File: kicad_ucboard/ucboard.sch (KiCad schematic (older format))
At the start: 180 parts, among them IC1 FT232RL, P1 Powerpath In, P10 BATTERY 2, P11 Timer8, P12 Timer20, P13 USB_B, P14 CAR-ID, P15 JTAG, P16 DIO, P17 ADC, P18 MPU-9250_EXT, P19 SFR08_I2C, P2 PWM_SERVO, P20 I2C2, P21 I2C3, P22 Serial Port, P23 5V, P24 5V, P25 3.3V, P26 UART4, P27 SPI2, P28 SPI4, P29 5V_Servo, P3 PWM_DRIVE, P4 BATT2_IN, P5 ADC12, P6 BATT2_REG_OUT, P7 Timer1, P8 Timer3, P9 Hal5, Q1 IRLML9301, Q2 IRLML6344, Q3 IRLML6344, Q4 IRLML9301, Q5 IRLML9301, Q6 IRLML6344, SW1 RESET, SW2 Button1, SW3 Button2, SW4 Button3, U1 STM32F303VE, U2 TEN_30-1212, U3 MCP6054, U4 TSR_1-2450, U5 TSR_1-2450, U6 LD1117_S33TR, U7 MPU-9250, U8 MAX3232, U9 25LC160A-I/SN, Y1 8MHz

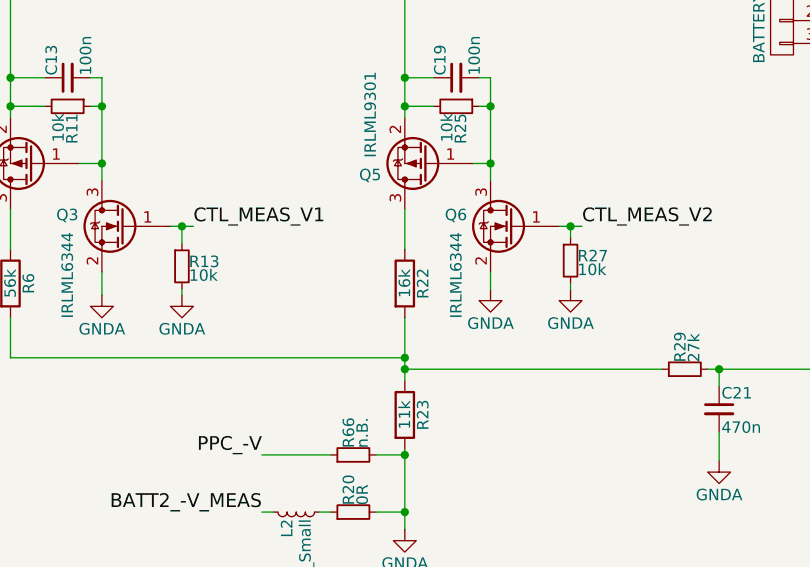
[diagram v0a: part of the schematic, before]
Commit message: - Bestellisten bis auf Spulen/Ferrite zur Entkopplung vervollständigt - Oberer Widerstand im Spannungsteiler an 7,2V von 16k auf 14k Reduziert (7,5V -> 3,3V)
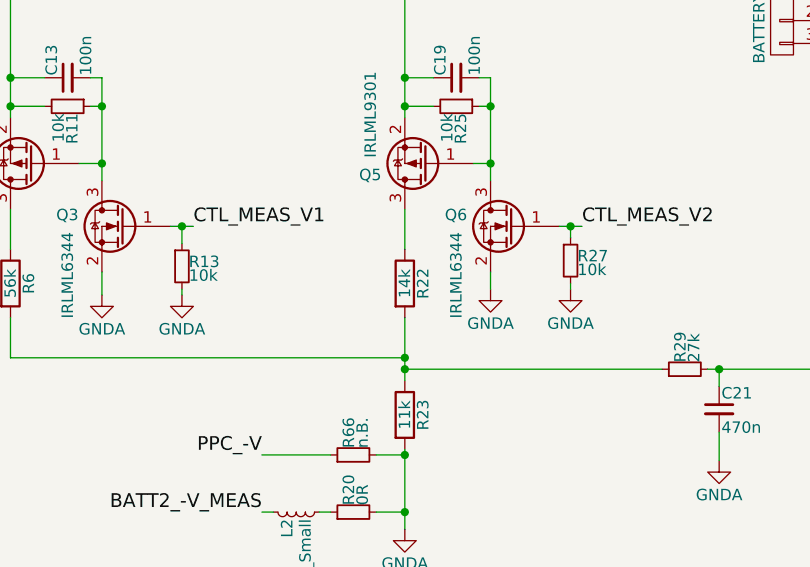
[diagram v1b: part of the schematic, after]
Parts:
- R22: value 16k -> 14k
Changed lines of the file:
@@
 EESchema Schematic File Version 2
-LIBS:ucboard-rescue
 LIBS:power
 LIBS:device
@@
 P 6675 4350
 F 0 "R22" V 6755 4350 50  0000 C CNN
-F 1 "16k" V 6675 4350 50  0000 C CNN
+F 1 "14k" V 6675 4350 50  0000 C CNN
 F 2 "Resistors_SMD:R_0603_HandSoldering" V 6605 4350 50  0001 C CNN
 F 3 "" H 6675 4350 50  0000 C CNN

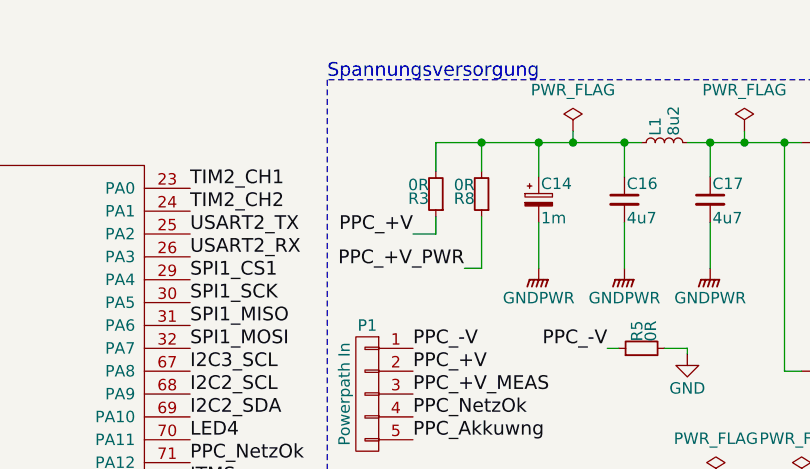
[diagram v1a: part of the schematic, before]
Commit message: - Wert von R3 von 0R auf n.B. geändert
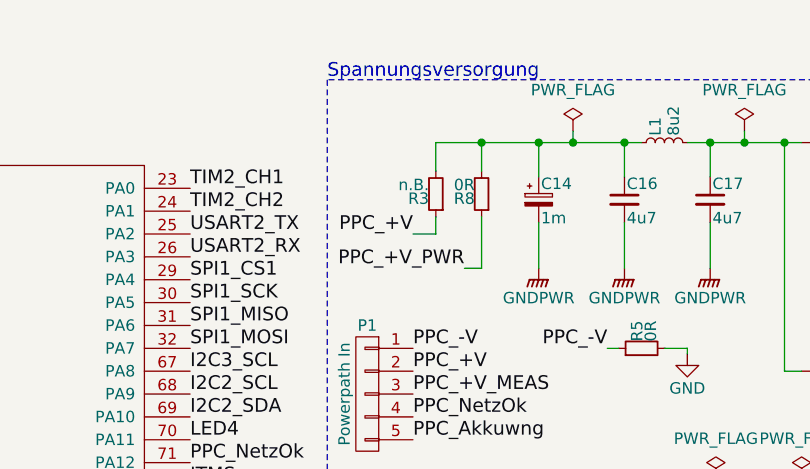
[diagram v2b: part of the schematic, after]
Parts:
- R3: value 0R -> n.B.
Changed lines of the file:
@@
 P 4825 1250
 F 0 "R3" H 4855 1270 50  0000 L CNN
-F 1 "0R" H 4855 1210 50  0000 L CNN
+F 1 "n.B." H 4855 1210 50  0000 L CNN
 F 2 "Resistors_SMD:R_0603_HandSoldering" H 4825 1250 50  0001 C CNN
 F 3 "" H 4825 1250 50  0000 C CNN

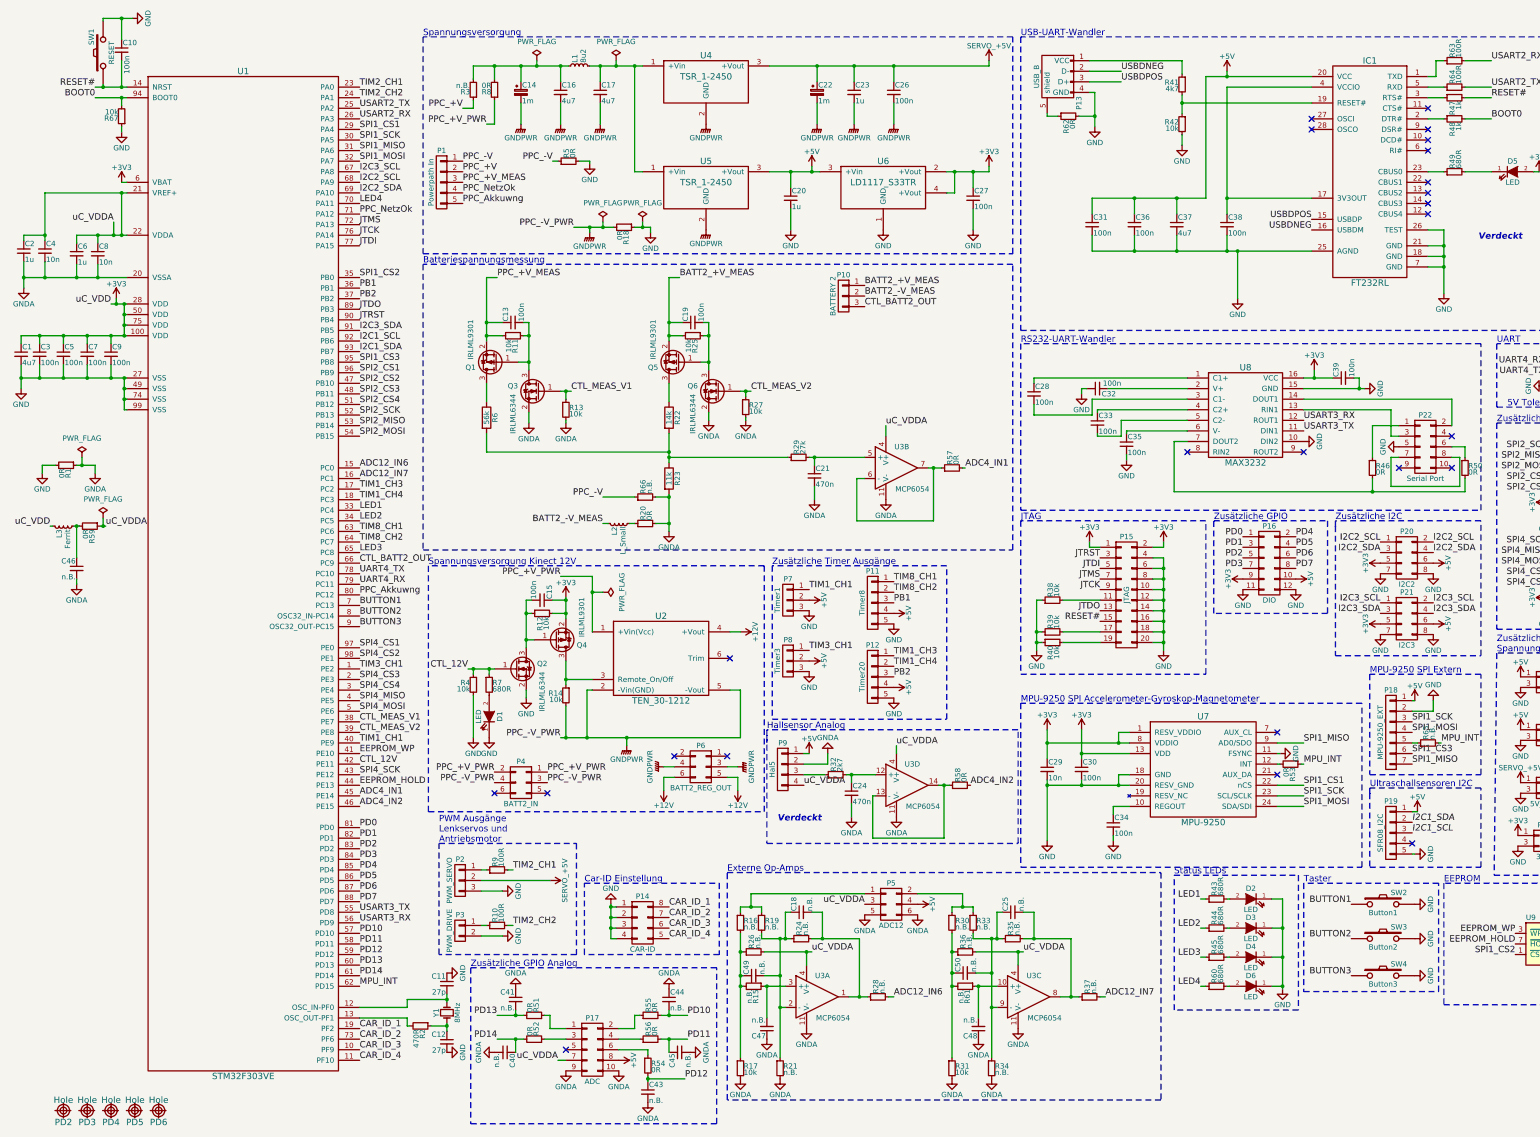
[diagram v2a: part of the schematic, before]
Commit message: Anpassen Schaltplan an aktuelle Bestückung: - R22: 56k anstelle 14k - C24: n.B. anstelle 470n - R68: 10k Pull-up für Hallsensor hinzugefügt
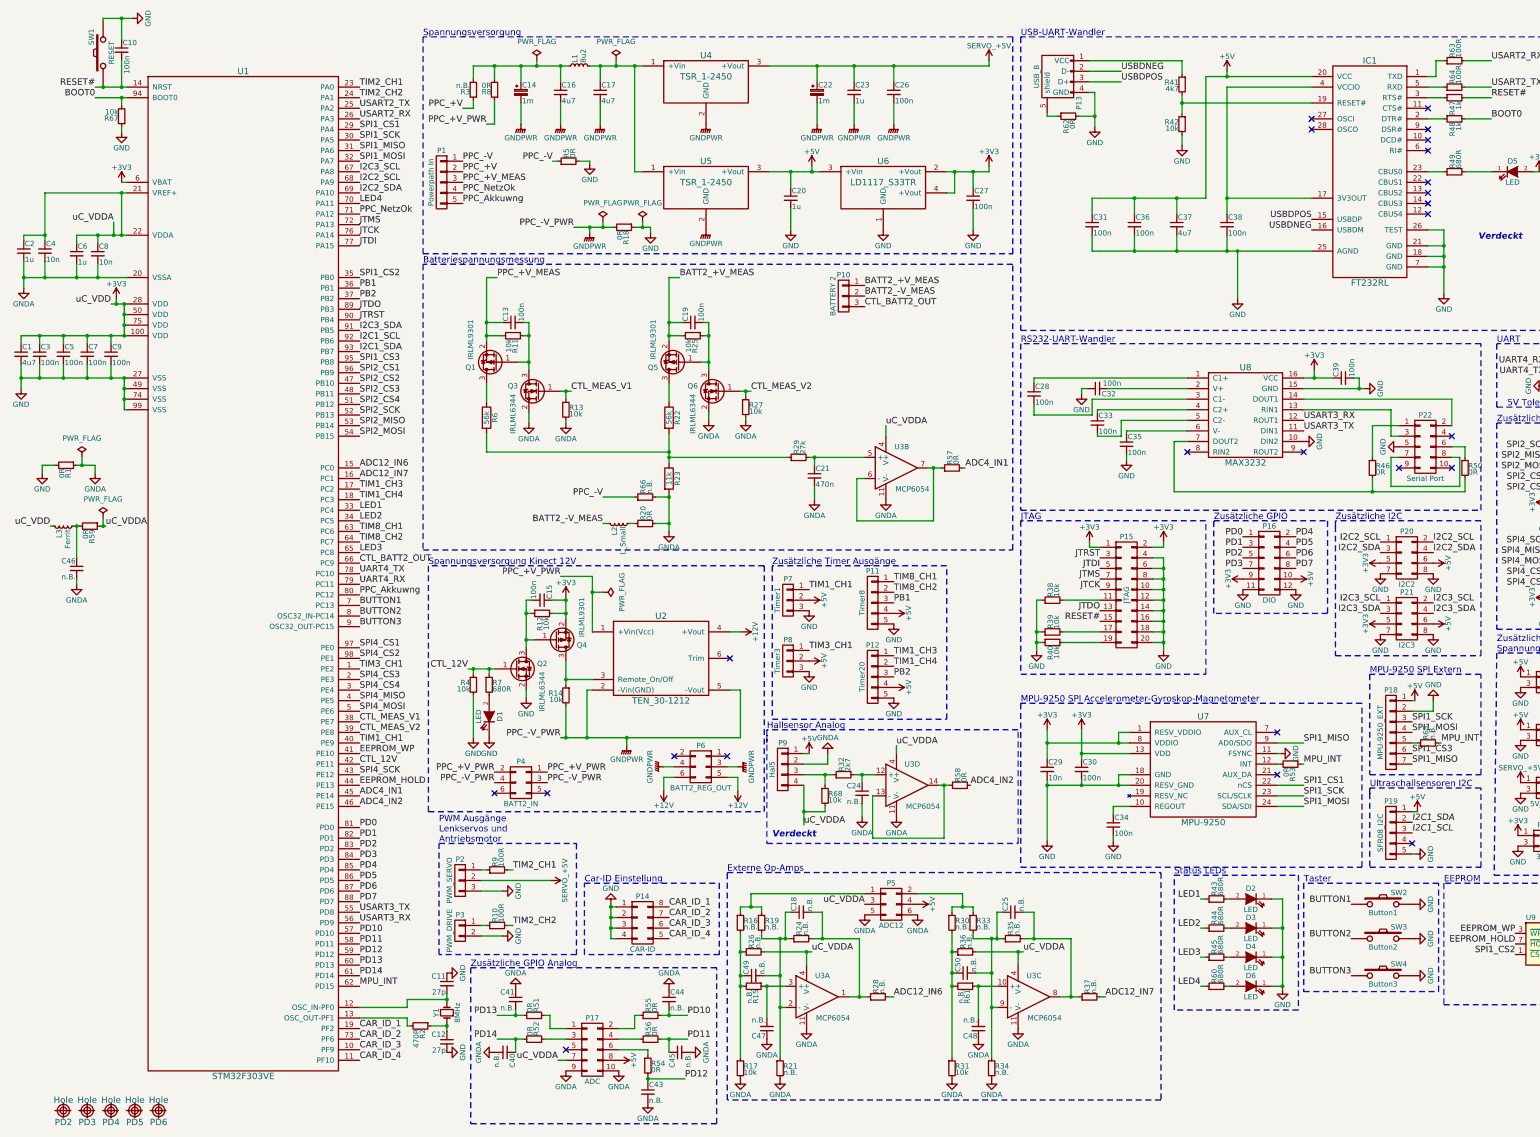
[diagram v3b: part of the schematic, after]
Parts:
- added R68: 10k, Resistors_SMD:R_0603_HandSoldering, symbol R_Small
- C24: value 470n -> n.B.
- R22: value 14k -> 56k; Supply (none) -> VEN:
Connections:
- net uC_VDDA: now also R68.2
- net at P9.3 (P3), R32.1: now also R68.1
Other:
- moved on the sheet: C24, R32

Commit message: In Kicad geänderte Bauteile "gerettet".
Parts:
- D1, D2, D3, D4, D5, D6: symbol LED -> LED-RESCUE-ucboard
- P13: symbol USB_B -> USB_B-RESCUE-ucboard
- U8: symbol MAX3232 -> MAX3232-RESCUE-ucboard

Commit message: Spezifikation D1-D6, L2+L3 nachgetragen
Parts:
- D1, D3: value LED -> 2mA, gn
- D2, D4, D5: value LED -> 2mA, re
- D6: value LED -> 2mA, or
- L2: value L_Small -> FB 600R; Supply (none) -> Farnell, 1635735
- L3: value Ferrit -> FB 600R; Supply (none) -> Farnell, 1635735
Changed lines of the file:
@@
 P 14650 2025
 F 0 "D5" H 14650 2125 50  0000 C CNN
-F 1 "LED" H 14650 1925 50  0000 C CNN
+F 1 "2mA, re" H 14650 1925 50  0000 C CNN
 F 2 "Custom:LED_0603_HandSoldering" H 14650 2025 50  0001 C CNN
 F 3 "" H 14650 2025 50  0000 C CNN
@@
 P 12175 9175
 F 0 "D3" H 12175 9275 50  0000 C CNN
-F 1 "LED" H 12175 9075 50  0000 C CNN
+F 1 "2mA, gn" H 12175 9075 50  0000 C CNN
 F 2 "Custom:LED_0603_HandSoldering" H 12175 9175 50  0001 C CNN
 F 3 "" H 12175 9175 50  0000 C CNN
@@
 P 12175 8900
 F 0 "D2" H 12175 9000 50  0000 C CNN
-F 1 "LED" H 12175 8800 50  0000 C CNN
+F 1 "2mA, re" H 12175 8800 50  0000 C CNN
 F 2 "Custom:LED_0603_HandSoldering" H 12175 8900 50  0001 C CNN
 F 3 "" H 12175 8900 50  0000 C CNN
@@
 P 12175 9450
 F 0 "D4" H 12175 9550 50  0000 C CNN
-F 1 "LED" H 12175 9350 50  0000 C CNN
+F 1 "2mA, re" H 12175 9350 50  0000 C CNN
 F 2 "Custom:LED_0603_HandSoldering" H 12175 9450 50  0001 C CNN
 F 3 "" H 12175 9450 50  0000 C CNN
@@
 P 4975 7175
 F 0 "D1" H 4975 7275 50  0000 C CNN
-F 1 "LED" H 4975 7075 50  0000 C CNN
+F 1 "2mA, gn" H 4975 7075 50  0000 C CNN
 F 2 "Custom:LED_0603_HandSoldering" H 4975 7175 50  0001 C CNN
 F 3 "" H 4975 7175 50  0000 C CNN
@@
 P 6200 5350
 F 0 "L2" H 6230 5390 50  0000 L CNN
-F 1 "L_Small" H 6230 5310 50  0000 L CNN
+F 1 "FB 600R" H 6230 5310 50  0000 L CNN
 F 2 "Resistors_SMD:R_0805_HandSoldering" H 6200 5350 50  0001 C CNN
 F 3 "" H 6200 5350 50  0000 C CNN
 F 4 "Spule oder Ferritperle" H 6200 5350 60  0001 C CNN "Spec"
+F 5 "Farnell, 1635735" H 6200 5350 60  0001 C CNN "Supply"
 	1    6200 5350
 	0    -1   1    0
@@
 P 950 5375
 F 0 "L3" H 980 5415 50  0000 L CNN
-F 1 "Ferrit" H 980 5335 50  0000 L CNN
+F 1 "FB 600R" H 980 5335 50  0000 L CNN
 F 2 "Resistors_SMD:R_0805_HandSoldering" H 950 5375 50  0001 C CNN
 F 3 "" H 950 5375 50  0000 C CNN
 F 4 "Spule oder Ferritperle" H 950 5375 60  0001 C CNN "Spec"
+F 5 "Farnell, 1635735" H 950 5375 60  0001 C CNN "Supply"
 	1    950  5375
 	0    -1   1    0
@@
 P 12175 9725
 F 0 "D6" H 12175 9825 50  0000 C CNN
-F 1 "LED" H 12175 9625 50  0000 C CNN
+F 1 "2mA, or" H 12175 9625 50  0000 C CNN
 F 2 "Custom:LED_0603_HandSoldering" H 12175 9725 50  0001 C CNN
 F 3 "" H 12175 9725 50  0000 C CNN

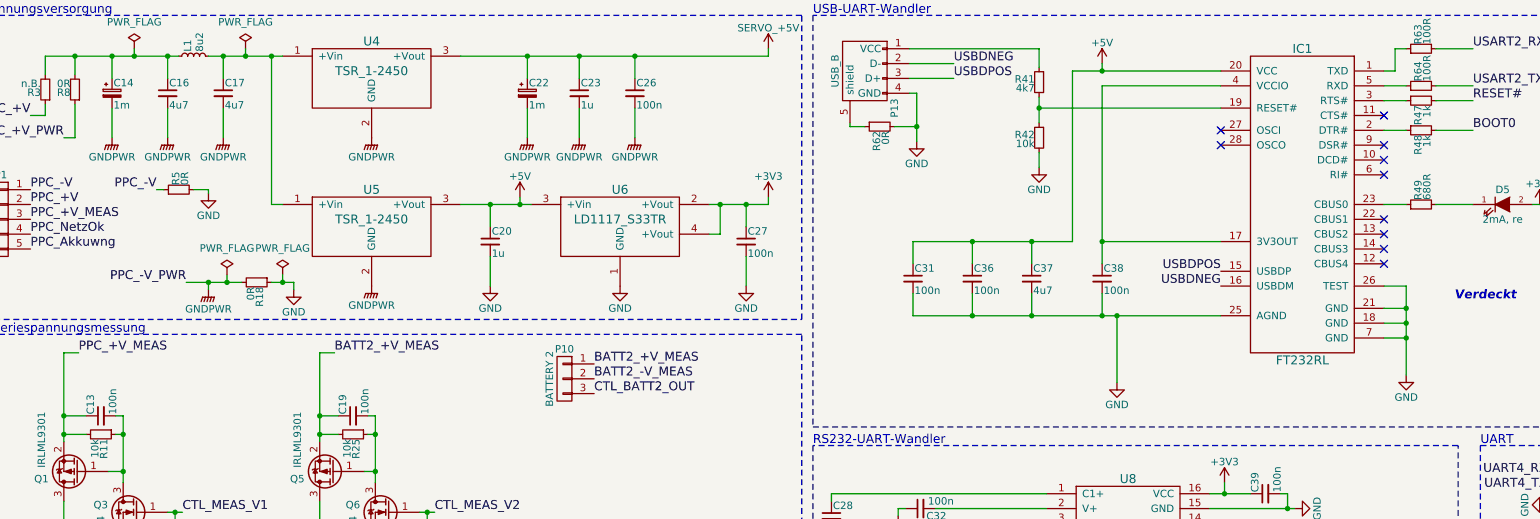
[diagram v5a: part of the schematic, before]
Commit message: - R47, R48 -> n.B. (Programmierung über USB wird nicht verwendet) - C13, C19 -> n.B. (Vermeiden des Einkoppelns von Störungen bei stark gestörten Versorgungsspannungen auf Masse)
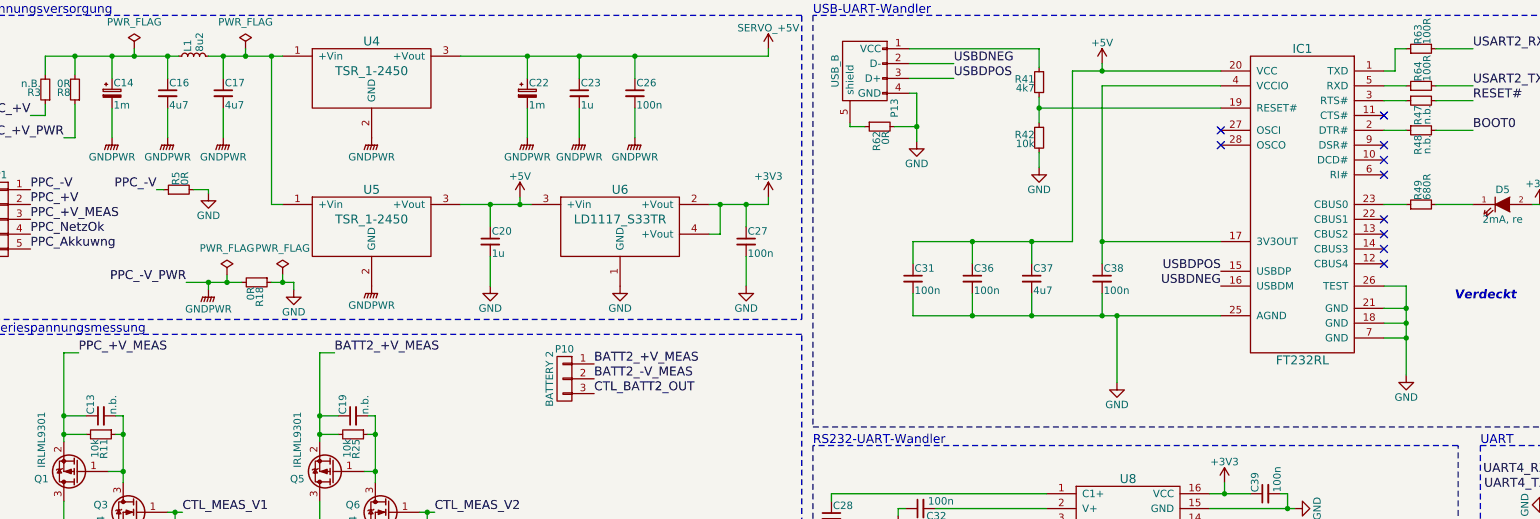
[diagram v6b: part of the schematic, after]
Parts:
- C13, C19: value 100n -> n.b.
- R47, R48: value 1k -> n.b.
